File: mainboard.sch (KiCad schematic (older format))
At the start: 36 parts, among them J1 105017-1001, J2 Conn_01x04_Female, J3 Conn_01x02_Female, J4 Conn_01x09_Female, J5 Conn_01x02_Female, J6 Conn_01x02_Female, J7 Conn_01x04_Female, J8 Conn_01x03_Female, Q1 AOD4184A, U1 ESP32-WROOM-32E_(16MB)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

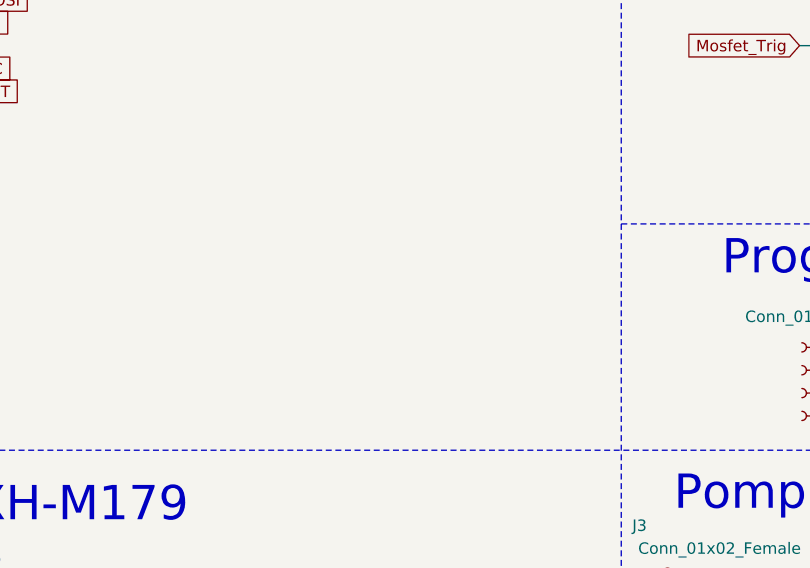
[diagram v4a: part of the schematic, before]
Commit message: mounting holes gefixt
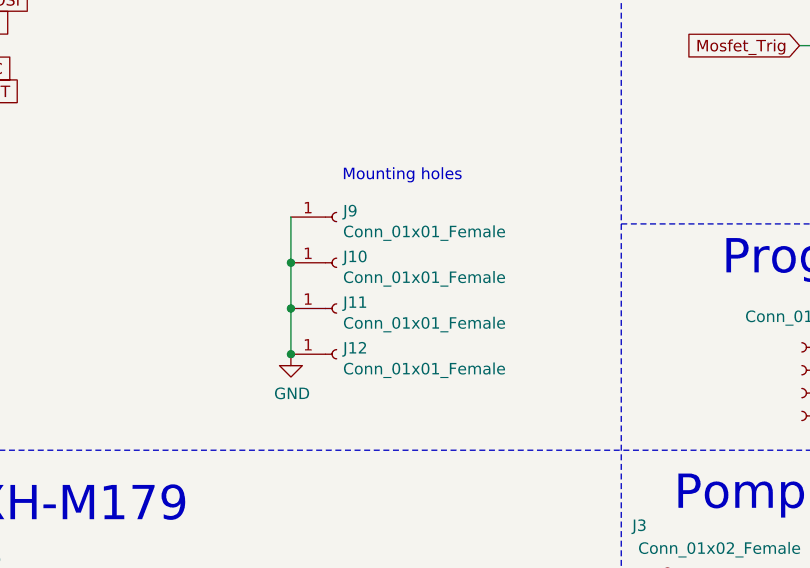
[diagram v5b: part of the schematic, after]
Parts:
- added J10, J11, J12, J9: Conn_01x01_Female, MountingHole:MountingHole_3.2mm_M3_ISO7380_Pad_TopBottom, symbol Connector:Conn_01x01_Female
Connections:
- net GND: now also J10.1 (Pin_1), J11.1 (Pin_1), J12.1 (Pin_1), J9.1 (Pin_1)
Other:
- note added: "Mounting holes"
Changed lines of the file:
@@
 NoConn ~ 2350 3550
 NoConn ~ 2350 3450
+$Comp
+L Connector:Conn_01x01_Female J9
+U 1 1 60709A36
+P 5725 4300
+F 0 "J9" H 5753 4326 50  0000 L CNN
+F 1 "Conn_01x01_Female" H 5753 4235 50  0000 L CNN
+F 2 "MountingHole:MountingHole_3.2mm_M3_ISO7380_Pad_TopBottom" H 5725 4300 50  0001 C CNN
+F 3 "~" H 5725 4300 50  0001 C CNN
+	1    5725 4300
+	1    0    0    -1
+$EndComp
+$Comp
+L Connector:Conn_01x01_Female J10
+U 1 1 6070D3CA
+P 5725 4500
+F 0 "J10" H 5753 4526 50  0000 L CNN
+F 1 "Conn_01x01_Female" H 5753 4435 50  0000 L CNN
+F 2 "MountingHole:MountingHole_3.2mm_M3_ISO7380_Pad_TopBottom" H 5725 4500 50  0001 C CNN
+F 3 "~" H 5725 4500 50  0001 C CNN
+	1    5725 4500
+	1    0    0    -1
+$EndComp
+$Comp
+L Connector:Conn_01x01_Female J11
+U 1 1 6070EC80
+P 5725 4700
+F 0 "J11" H 5753 4726 50  0000 L CNN
+F 1 "Conn_01x01_Female" H 5753 4635 50  0000 L CNN
+F 2 "MountingHole:MountingHole_3.2mm_M3_ISO7380_Pad_TopBottom" H 5725 4700 50  0001 C CNN
+F 3 "~" H 5725 4700 50  0001 C CNN
+	1    5725 4700
+	1    0    0    -1
+$EndComp
+$Comp
+L Connector:Conn_01x01_Female J12
+U 1 1 607103E8
+P 5725 4900
+F 0 "J12" H 5753 4926 50  0000 L CNN
+F 1 "Conn_01x01_Female" H 5753 4835 50  0000 L CNN
+F 2 "MountingHole:MountingHole_3.2mm_M3_ISO7380_Pad_TopBottom" H 5725 4900 50  0001 C CNN
+F 3 "~" H 5725 4900 50  0001 C CNN
+	1    5725 4900
+	1    0    0    -1
+$EndComp
+Wire Wire Line
+	5525 4700 5525 4500
+Wire Wire Line
+	5525 4300 5525 4500
+Connection ~ 5525 4500
+Wire Wire Line
+	5525 4900 5525 4700
+Connection ~ 5525 4700
+Text Notes 5750 4150 0    50   ~ 0
+Mounting holes
+$Comp
+L power:GND #PWR?
+U 1 1 6072A593
+P 5525 4900
+F 0 "#PWR?" H 5525 4650 50  0001 C CNN
+F 1 "GND" H 5530 4727 50  0000 C CNN
+F 2 "" H 5525 4900 50  0001 C CNN
+F 3 "" H 5525 4900 50  0001 C CNN
+	1    5525 4900
+	1    0    0    -1
+$EndComp
+Connection ~ 5525 4900
 $EndSCHEMATC

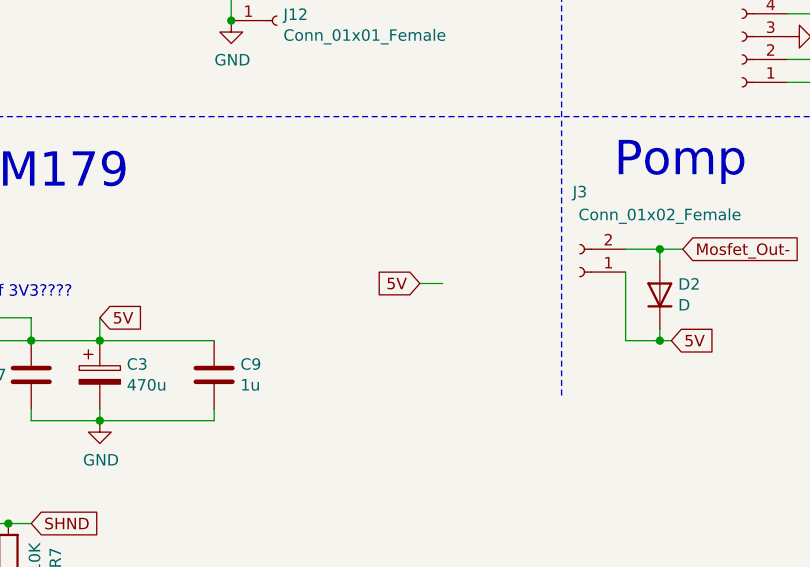
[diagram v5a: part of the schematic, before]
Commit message: de zwevende 5v is weg
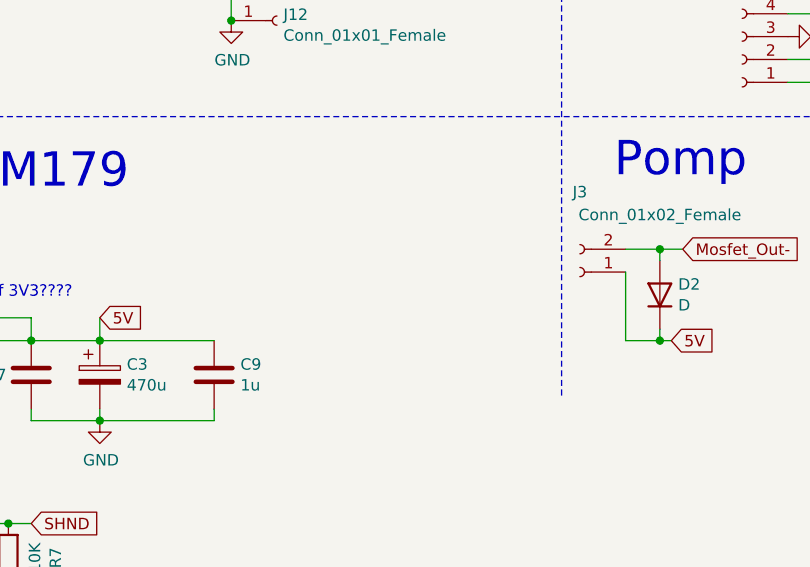
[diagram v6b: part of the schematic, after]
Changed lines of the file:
@@
 Wire Wire Line
 	8050 3550 8250 3550
-Text GLabel 6350 6050 0    50   Input ~ 0
-5V
 $Comp
 L Device:D D2
@@
 $EndComp
 Wire Wire Line
-	6350 6050 6450 6050
-Wire Wire Line
 	7750 2900 8450 2900

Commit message: finale versie pcb
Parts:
- J10, J11, J12, J9: footprint MountingHole:MountingHole_3.2mm_M3_ISO7380_Pad_TopBottom -> MountingHole:MountingHole_3.2mm_M3_DIN965
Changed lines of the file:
@@
 F 0 "J9" H 5753 4326 50  0000 L CNN
 F 1 "Conn_01x01_Female" H 5753 4235 50  0000 L CNN
-F 2 "MountingHole:MountingHole_3.2mm_M3_ISO7380_Pad_TopBottom" H 5725 4300 50  0001 C CNN
+F 2 "MountingHole:MountingHole_3.2mm_M3_DIN965" H 5725 4300 50  0001 C CNN
 F 3 "~" H 5725 4300 50  0001 C CNN
 	1    5725 4300
@@
 F 0 "J10" H 5753 4526 50  0000 L CNN
 F 1 "Conn_01x01_Female" H 5753 4435 50  0000 L CNN
-F 2 "MountingHole:MountingHole_3.2mm_M3_ISO7380_Pad_TopBottom" H 5725 4500 50  0001 C CNN
+F 2 "MountingHole:MountingHole_3.2mm_M3_DIN965" H 5725 4500 50  0001 C CNN
 F 3 "~" H 5725 4500 50  0001 C CNN
 	1    5725 4500
@@
 F 0 "J11" H 5753 4726 50  0000 L CNN
 F 1 "Conn_01x01_Female" H 5753 4635 50  0000 L CNN
-F 2 "MountingHole:MountingHole_3.2mm_M3_ISO7380_Pad_TopBottom" H 5725 4700 50  0001 C CNN
+F 2 "MountingHole:MountingHole_3.2mm_M3_DIN965" H 5725 4700 50  0001 C CNN
 F 3 "~" H 5725 4700 50  0001 C CNN
 	1    5725 4700
@@
 F 0 "J12" H 5753 4926 50  0000 L CNN
 F 1 "Conn_01x01_Female" H 5753 4835 50  0000 L CNN
-F 2 "MountingHole:MountingHole_3.2mm_M3_ISO7380_Pad_TopBottom" H 5725 4900 50  0001 C CNN
+F 2 "MountingHole:MountingHole_3.2mm_M3_DIN965" H 5725 4900 50  0001 C CNN
 F 3 "~" H 5725 4900 50  0001 C CNN
 	1    5725 4900
@@
 Mounting holes
 $Comp
-L power:GND #PWR?
+L power:GND #PWR0104
 U 1 1 6072A593
 P 5525 4900
-F 0 "#PWR?" H 5525 4650 50  0001 C CNN
+F 0 "#PWR0104" H 5525 4650 50  0001 C CNN
 F 1 "GND" H 5530 4727 50  0000 C CNN
 F 2 "" H 5525 4900 50  0001 C CNN
